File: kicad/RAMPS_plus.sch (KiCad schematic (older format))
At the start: 20 parts, among them CON1 CON10, CON2 CON8, CON3 CON8, CON4 CON8, CON5 CON6, CON6 CON8, CON7 CON8, CON8 CON18x2

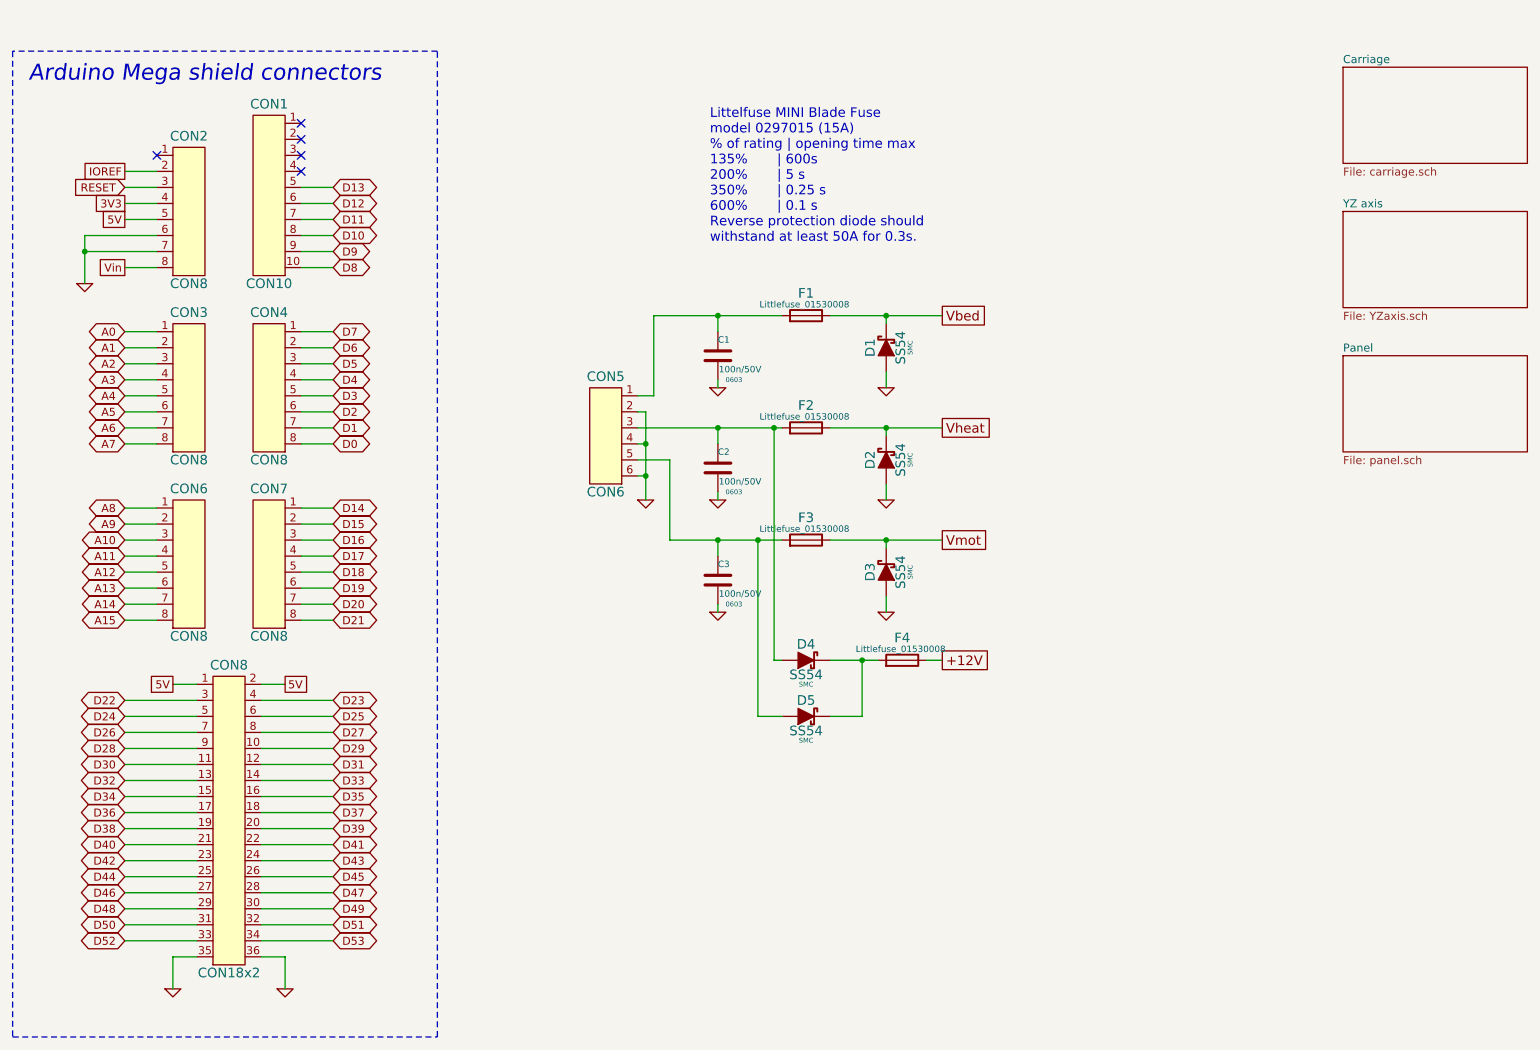
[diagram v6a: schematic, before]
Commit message: Add panel connectors. Minor ERC fixes.
References: #11
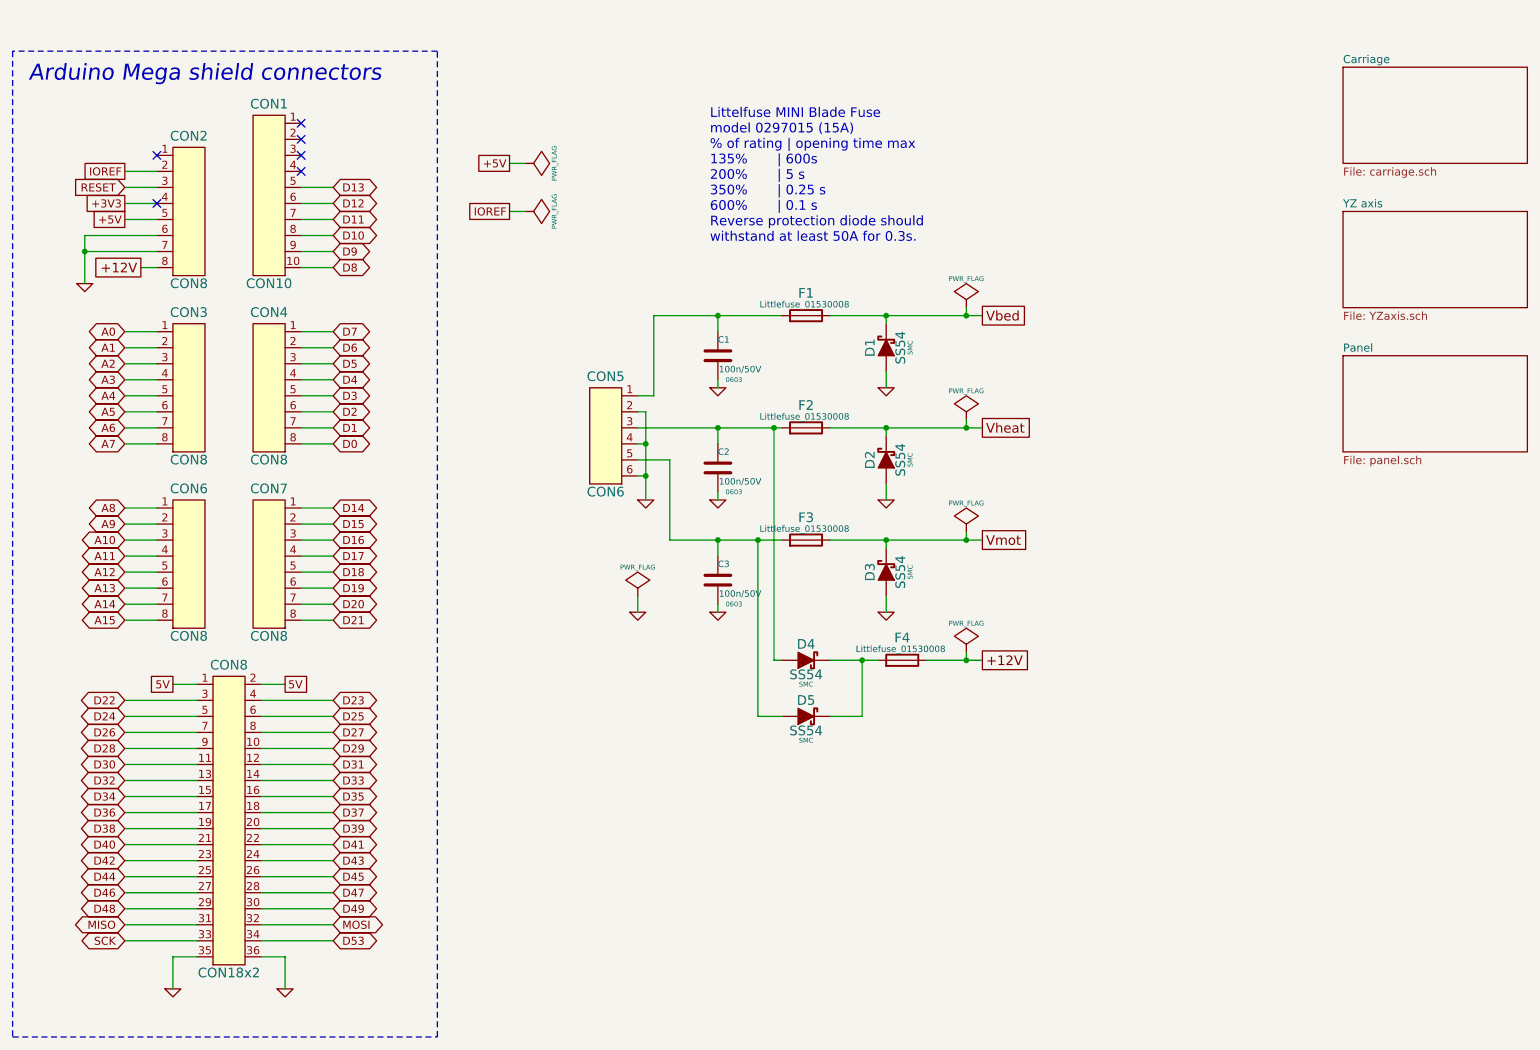
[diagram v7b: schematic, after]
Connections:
- net Vin is gone; now on net +12V: CON2.8
- net 5V: no longer CON2.5
- net 3V3 renamed +3V3
- net D50 renamed MISO
- net D51 renamed MOSI
- net D52 renamed SCK
- new net +5V: CON2.5
- no-connect marks 5 -> 6
